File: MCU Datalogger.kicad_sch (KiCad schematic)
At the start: 25 parts, among them U1 24LC1025, U2 DS1337S_, U3 24LC1025, U4 ATMEGA328P-AU, Y1 32.768 MHz, Y2 16 MHz

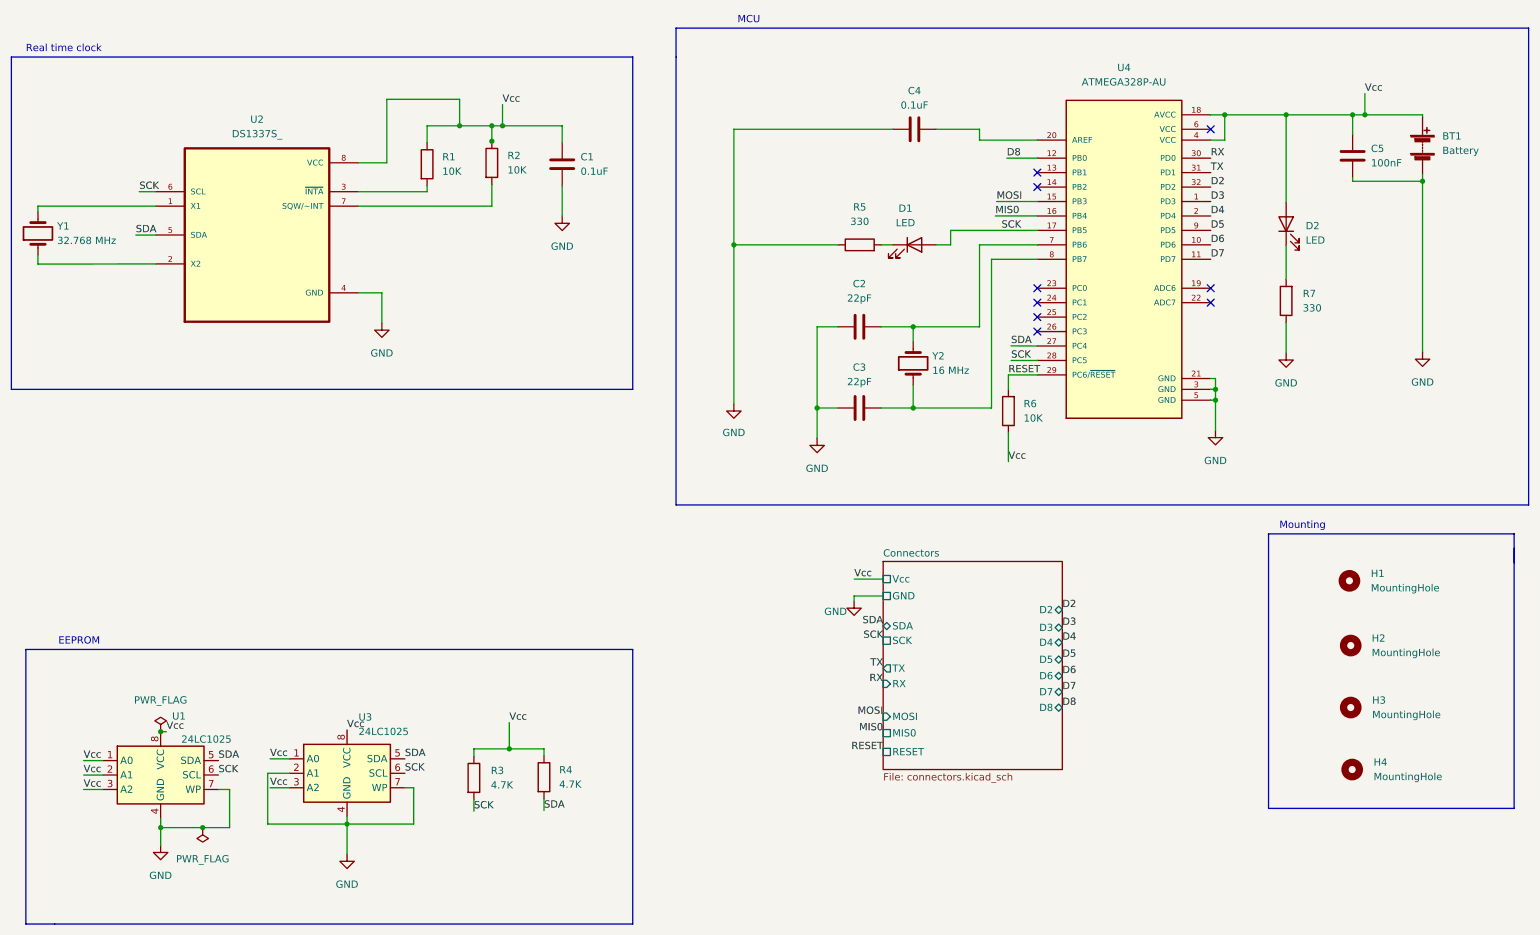
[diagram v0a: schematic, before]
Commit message: Fixed two defects in the schematic.
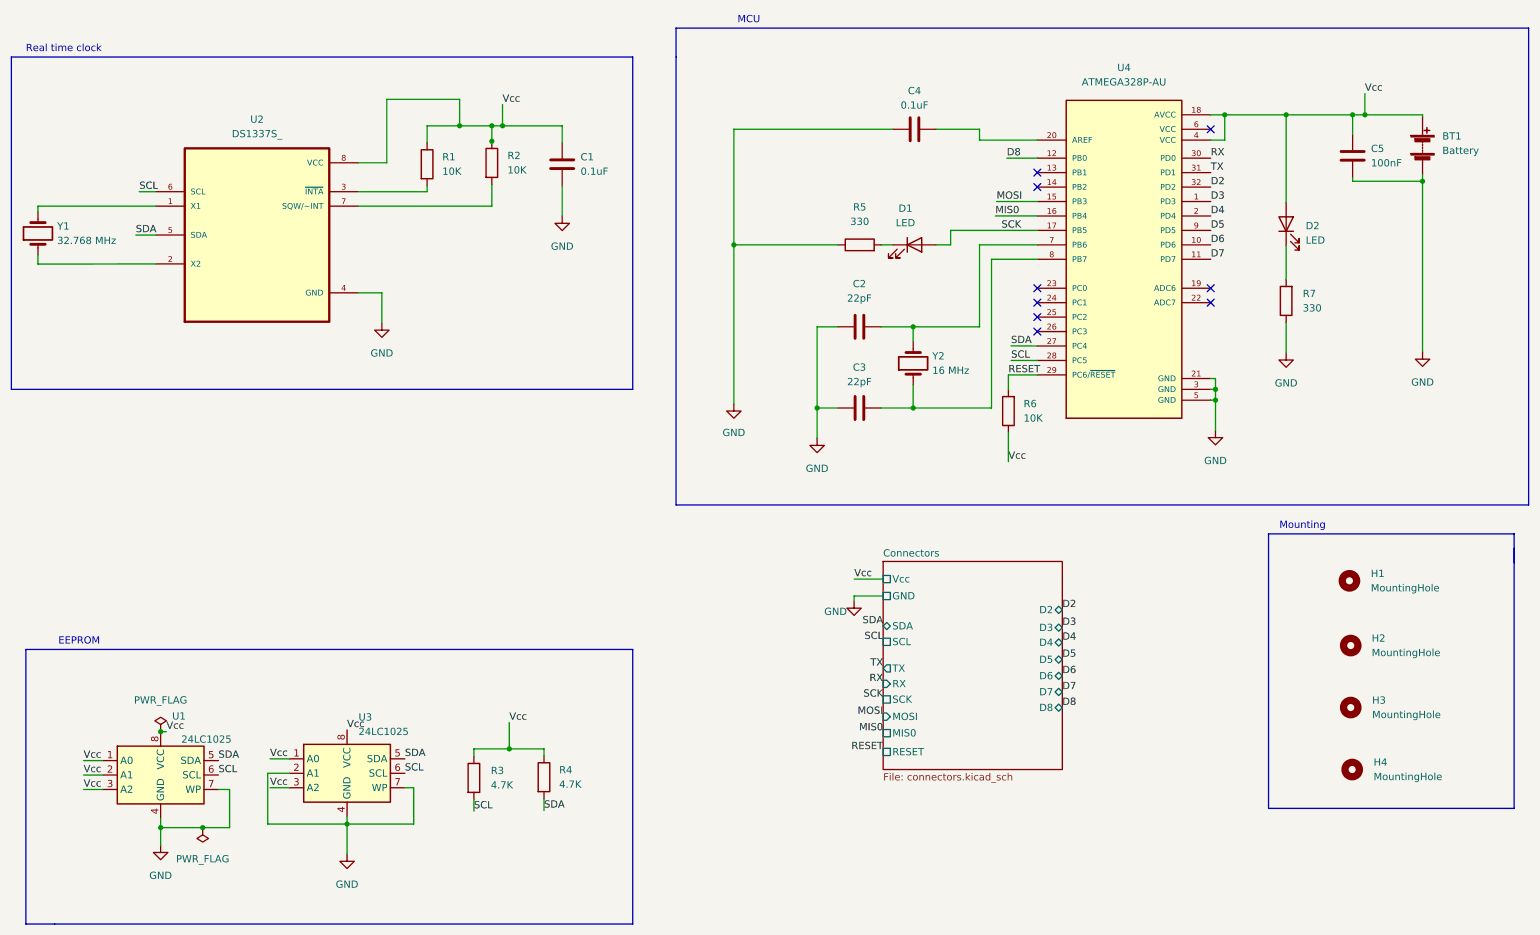
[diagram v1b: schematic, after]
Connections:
- net SCK: no longer R3.2, U1.6 (SCL), U2.6 (SCL), U3.6 (SCL), U4.28 (PC5)
- new net SCL: R3.2, U1.6 (SCL), U2.6 (SCL), U3.6 (SCL), U4.28 (PC5)
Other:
- sheet Connectors ports: added SCL; removed none
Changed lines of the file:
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@@
     (effects (font (size 1.27 1.27)) (justify left bottom))
   )
-  (label "SCK" (at 37.719 46.5328 0)
-    (effects (font (size 1.27 1.27)) (justify left bottom))
-  )
-  (label "SCK" (at 190.9826 76.2 0)
+  (label "SCL" (at 37.719 46.5328 0)
+    (effects (font (size 1.27 1.27)) (justify left bottom))
+  )
+  (label "SCL" (at 190.9826 76.2 0)
     (effects (font (size 1.27 1.27)) (justify left bottom))
   )
@@
     (effects (font (size 1.27 1.27)) (justify left bottom))
   )
-  (label "SCK" (at 51.6382 149.0726 0)
+  (label "SCL" (at 51.6382 149.0726 0)
     (effects (font (size 1.27 1.27)) (justify left bottom))
   )
@@
     (effects (font (size 1.27 1.27)) (justify left bottom))
   )
+  (label "SCL" (at 168.4782 125.6538 180)
+    (effects (font (size 1.27 1.27)) (justify right bottom))
+  )
   (label "SDA" (at 37.1094 54.1528 0)
     (effects (font (size 1.27 1.27)) (justify left bottom))
@@
     (effects (font (size 1.27 1.27)) (justify left bottom))
   )
-  (label "SCK" (at 168.4782 125.4506 180)
+  (label "SCK" (at 168.4782 135.7884 180)
     (effects (font (size 1.27 1.27)) (justify right bottom))
   )
@@
     (effects (font (size 1.27 1.27)) (justify left bottom))
   )
-  (label "SCK" (at 96.5454 155.4226 0)
+  (label "SCL" (at 96.5454 155.4226 0)
     (effects (font (size 1.27 1.27)) (justify left bottom))
   )
@@
     (effects (font (size 1.27 1.27)) (justify right bottom))
   )
-  (label "SCK" (at 84.4042 148.7678 0)
+  (label "SCL" (at 84.4042 148.7678 0)
     (effects (font (size 1.27 1.27)) (justify left bottom))
   )
@@
       (effects (font (size 1.27 1.27)) (justify left))
     )
-    (pin "SCK" passive (at 168.4782 125.4506 180)
+    (pin "SCK" passive (at 168.4782 135.7884 180)
       (effects (font (size 1.27 1.27)) (justify left))
     )
@@
       (effects (font (size 1.27 1.27)) (justify left))
     )
+    (pin "SCL" passive (at 168.4782 125.6538 180)
+      (effects (font (size 1.27 1.27)) (justify left))
+    )
